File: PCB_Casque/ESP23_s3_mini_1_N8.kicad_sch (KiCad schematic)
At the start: 11 parts, among them SW3 SW_Push, SW5 SW_Push, U3 ESP32-S3-MINI-1

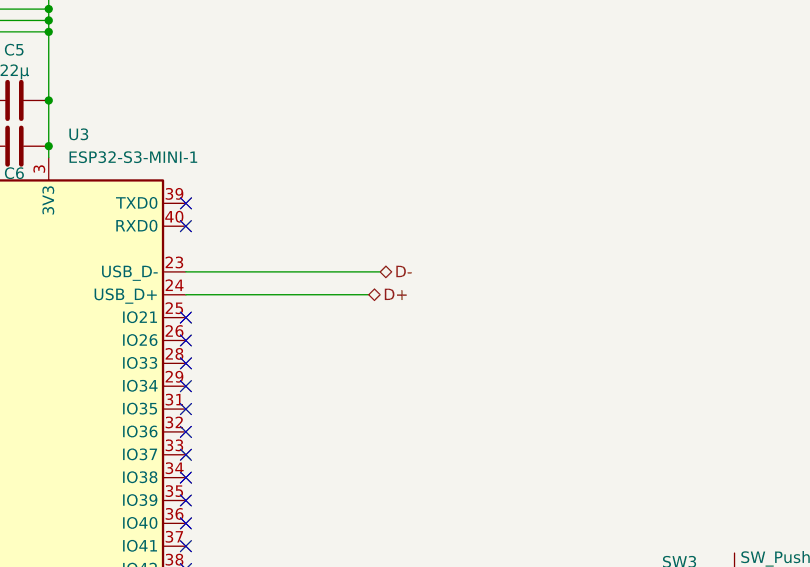
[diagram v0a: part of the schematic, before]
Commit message: ajout du PCB version final + elt du design
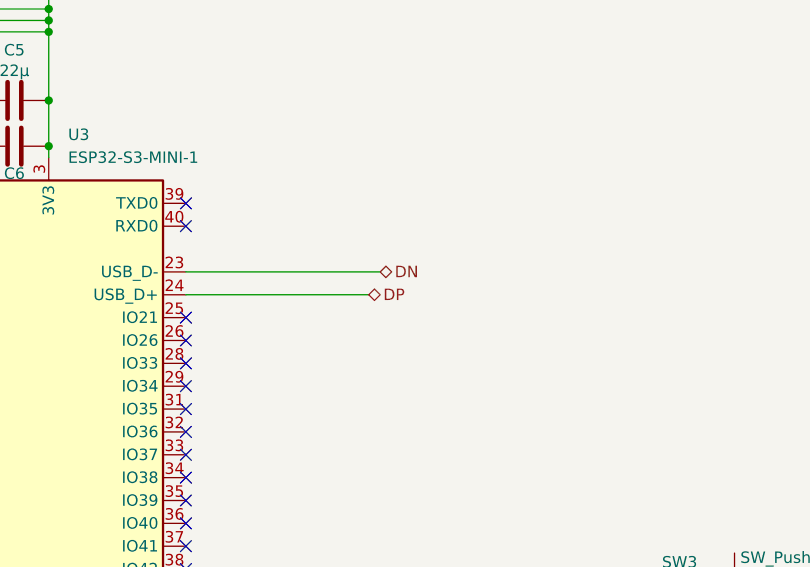
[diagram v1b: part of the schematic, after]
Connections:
- net D+ renamed DP
- net D- renamed DN
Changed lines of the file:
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@@
 		)
 	)
-	(hierarchical_label "D-"
+	(hierarchical_label "DN"
 		(shape bidirectional)
 		(at 175.26 73.66 0)
@@
 		)
 	)
-	(hierarchical_label "D+"
+	(hierarchical_label "DP"
 		(shape bidirectional)
 		(at 173.99 76.2 0)
